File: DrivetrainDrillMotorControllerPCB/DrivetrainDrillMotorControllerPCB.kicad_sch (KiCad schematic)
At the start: 42 parts, among them J1 DC-005-5A-2.0, J10 Conn_01x02_Socket, J11 Conn_01x02_Socket, J12 Conn_01x02_Socket, J13 Conn_01x02_Socket, J14 Conn_01x02_Socket, J15 Conn_01x02_Socket, J16 Conn_01x02_Socket, J2 Conn_01x02_Socket, J3 Conn_01x02_Socket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

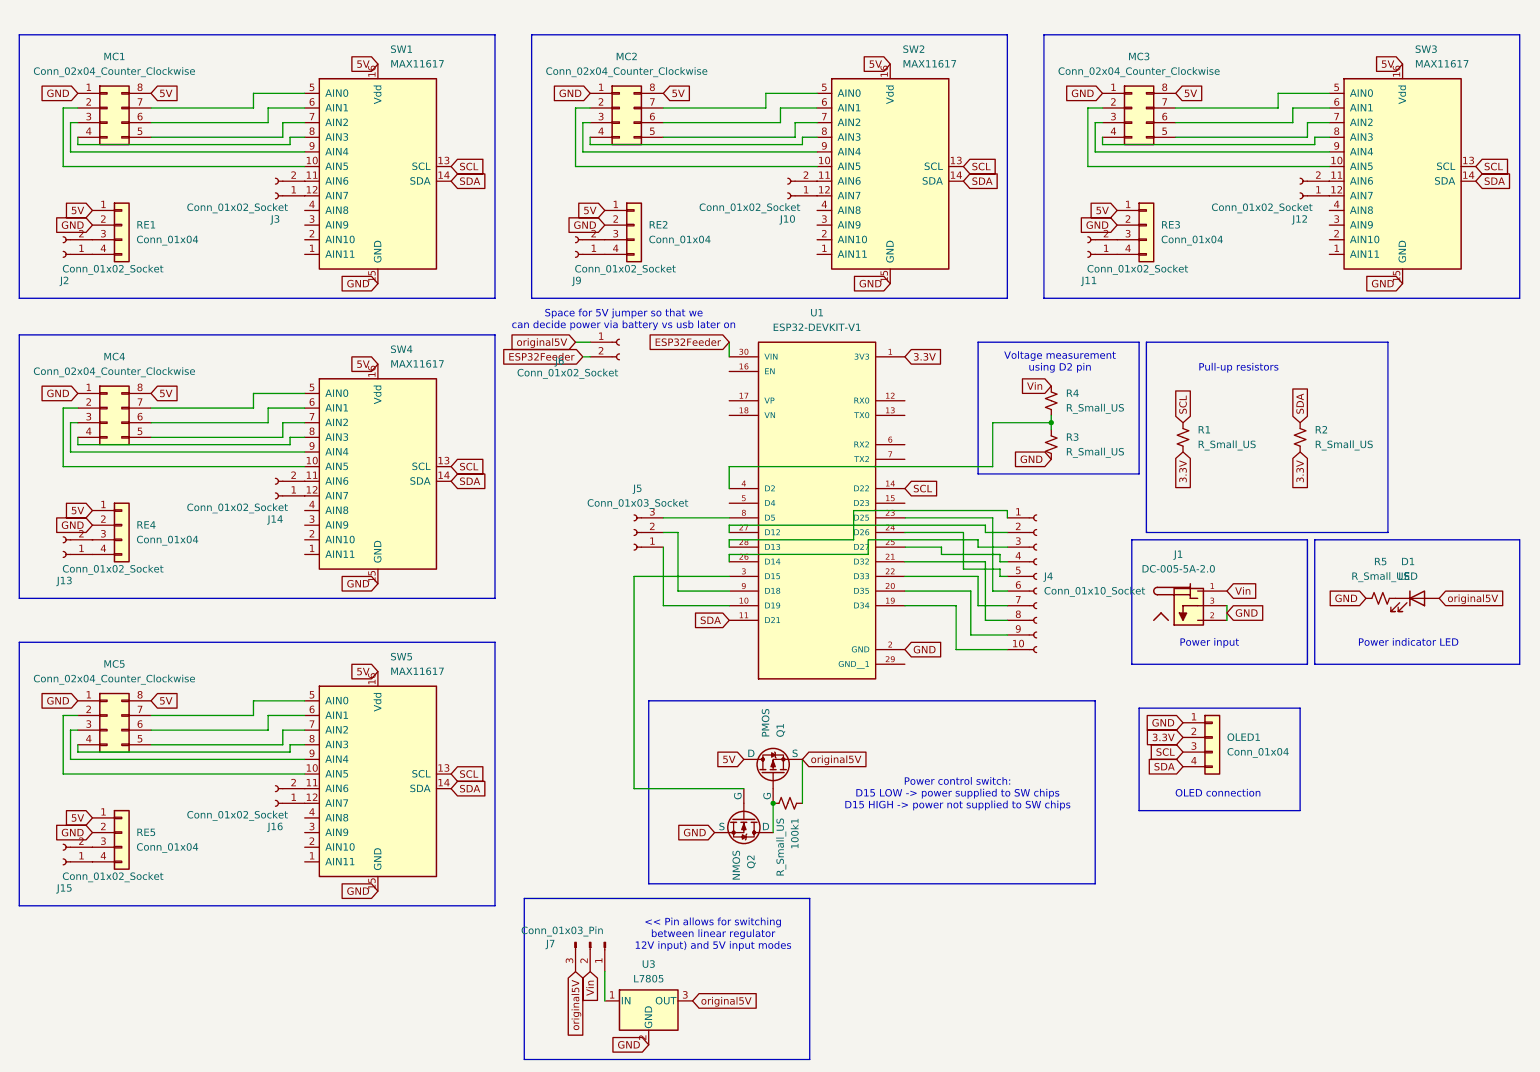
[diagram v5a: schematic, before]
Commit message: Added GND pin, connected REs to SW
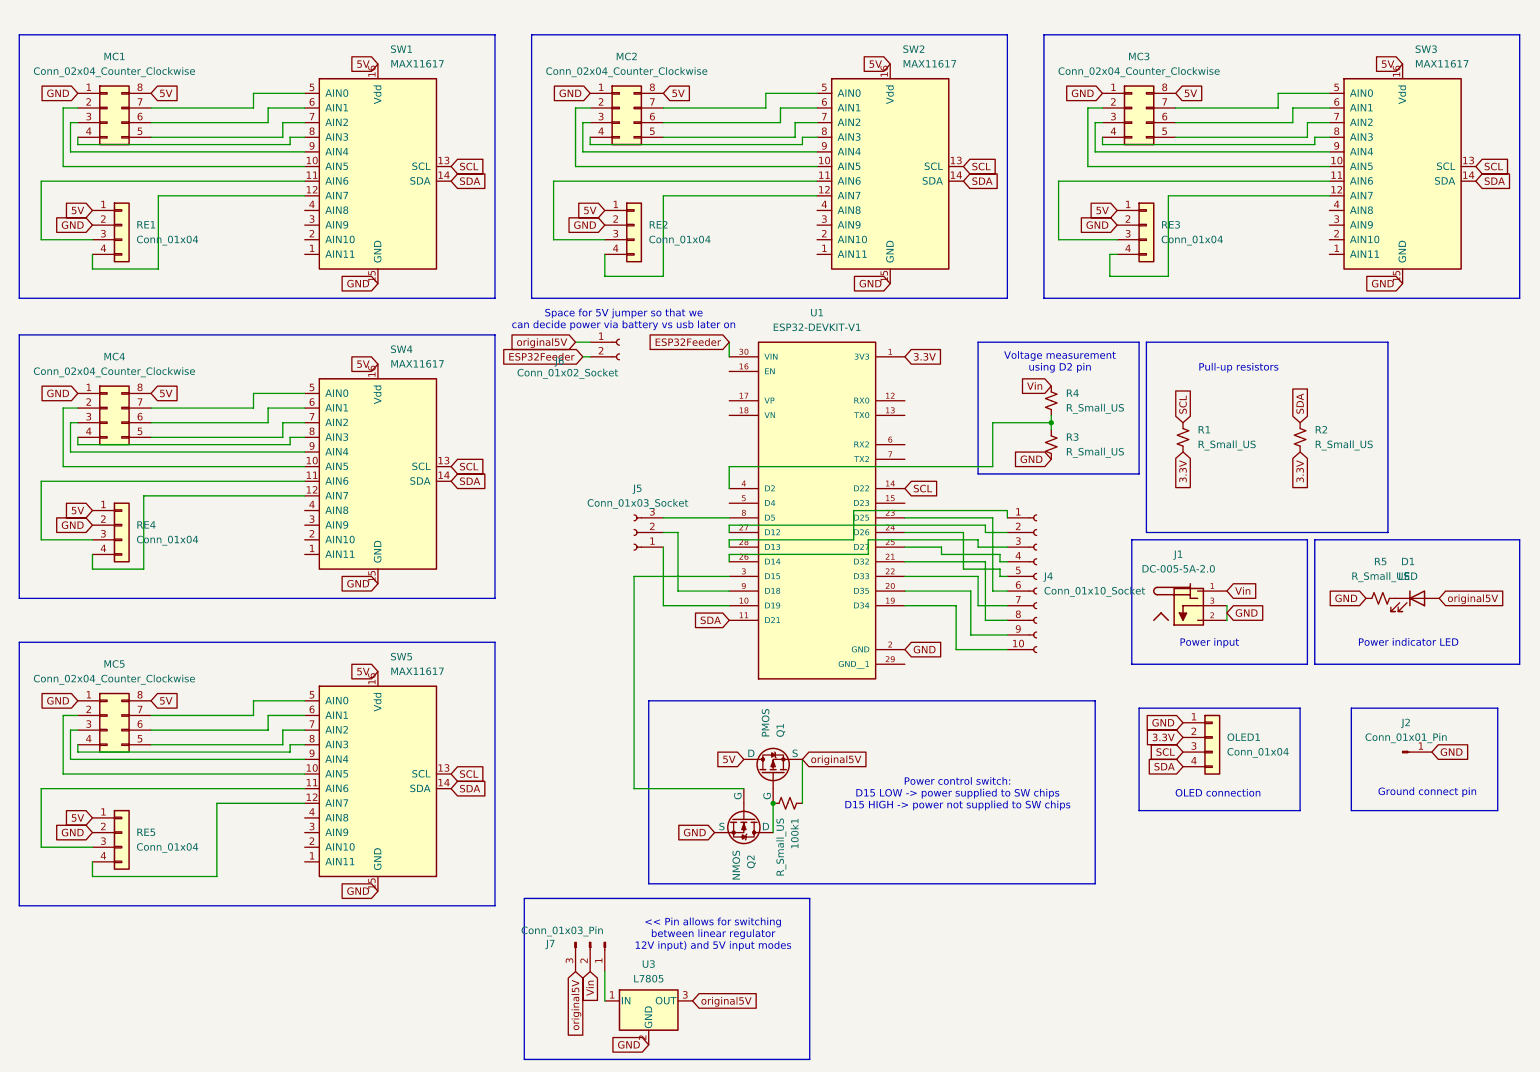
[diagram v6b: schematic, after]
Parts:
- removed J10, J11, J12, J13, J14, J15, J16, J2, J3, J9: Conn_01x02_Socket, Connector_PinHeader_2.54mm:PinHeader_1x02_P2.54mm_Vertical, symbol Connector:Conn_01x02_Socket
- added J2: Conn_01x01_Pin, Connector_PinHeader_2.54mm:PinHeader_1x01_P2.54mm_Vertical, symbol Connector:Conn_01x01_Pin
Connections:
- net GND: now also J2.1 (Pin_1)
- net at RE2.3 (Pin_3): now also SW2.11 (AIN6)
- net at RE2.4 (Pin_4): now also SW2.12 (AIN7)
- net at SW4.11 (AIN6): now also RE4.3 (Pin_3)
- net at SW4.12 (AIN7): now also RE4.4 (Pin_4)
- net at RE3.4 (Pin_4): now also SW3.12 (AIN7)
- net at RE3.3 (Pin_3): now also SW3.11 (AIN6)
- net at RE5.4 (Pin_4): now also SW5.12 (AIN7)
- net at RE5.3 (Pin_3): now also SW5.11 (AIN6)
- net at RE1.3 (Pin_3): now also SW1.11 (AIN6)
- net at RE1.4 (Pin_4): now also SW1.12 (AIN7)
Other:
- note added: "Ground connect pin"

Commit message: Misc motor control pcb stuff
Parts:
- removed 100k1: R_Small_US, Connector_PinHeader_2.54mm:PinHeader_1x02_P2.54mm_Vertical, symbol Device:R_Small_US
- removed MC1, MC2, MC3, MC4, MC5: Conn_02x04_Counter_Clockwise, Connector_IDC:IDC-Header_2x04_P2.54mm_Vertical, symbol Connector_Generic:Conn_02x04_Counter_Clockwise
- removed Q1: PMOS, Connector_PinHeader_2.54mm:PinHeader_1x03_P2.54mm_Vertical, symbol Simulation_SPICE:PMOS
- removed Q2: NMOS, Connector_PinHeader_2.54mm:PinHeader_1x03_P2.54mm_Vertical, symbol Simulation_SPICE:NMOS
- removed RE1, RE2, RE3, RE4, RE5: Conn_01x04, Connector_PinHeader_2.54mm:PinHeader_1x04_P2.54mm_Vertical, symbol Connector_Generic:Conn_01x04
- removed SW1, SW2, SW3, SW4, SW5: MAX11617, SerialWombat:sw_pcb0029, symbol Analog_ADC:MAX11617
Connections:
- net original5V is gone; now on net 5V: D1.2 (A), J6.1 (Pin_1), J7.3 (Pin_3), U3.3 (OUT)
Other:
- added sheet OneMotor (OneMotor.kicad_sch)
- added sheet OneMotor1 (OneMotor.kicad_sch)
- added sheet OneMotor2 (OneMotor.kicad_sch)
- added sheet OneMotor3 (OneMotor.kicad_sch)
- added sheet OneMotor4 (OneMotor.kicad_sch)
- note removed: "Power control switch: D15 LOW -> power supplied to SW chips D15 HIGH -> power not supplied to SW chips"
